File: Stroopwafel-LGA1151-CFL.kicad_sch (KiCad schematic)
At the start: 0 parts

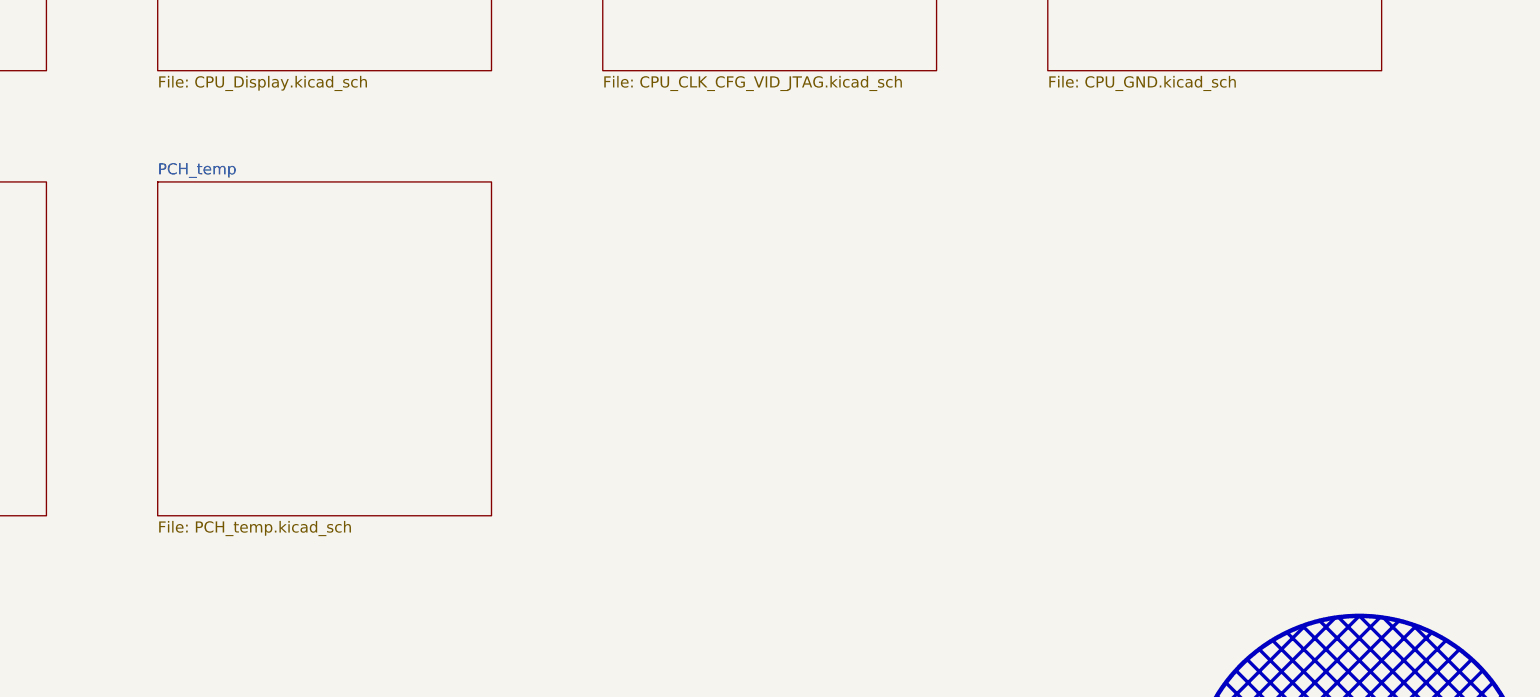
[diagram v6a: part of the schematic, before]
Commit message: Moved PCH symbols to their own pages
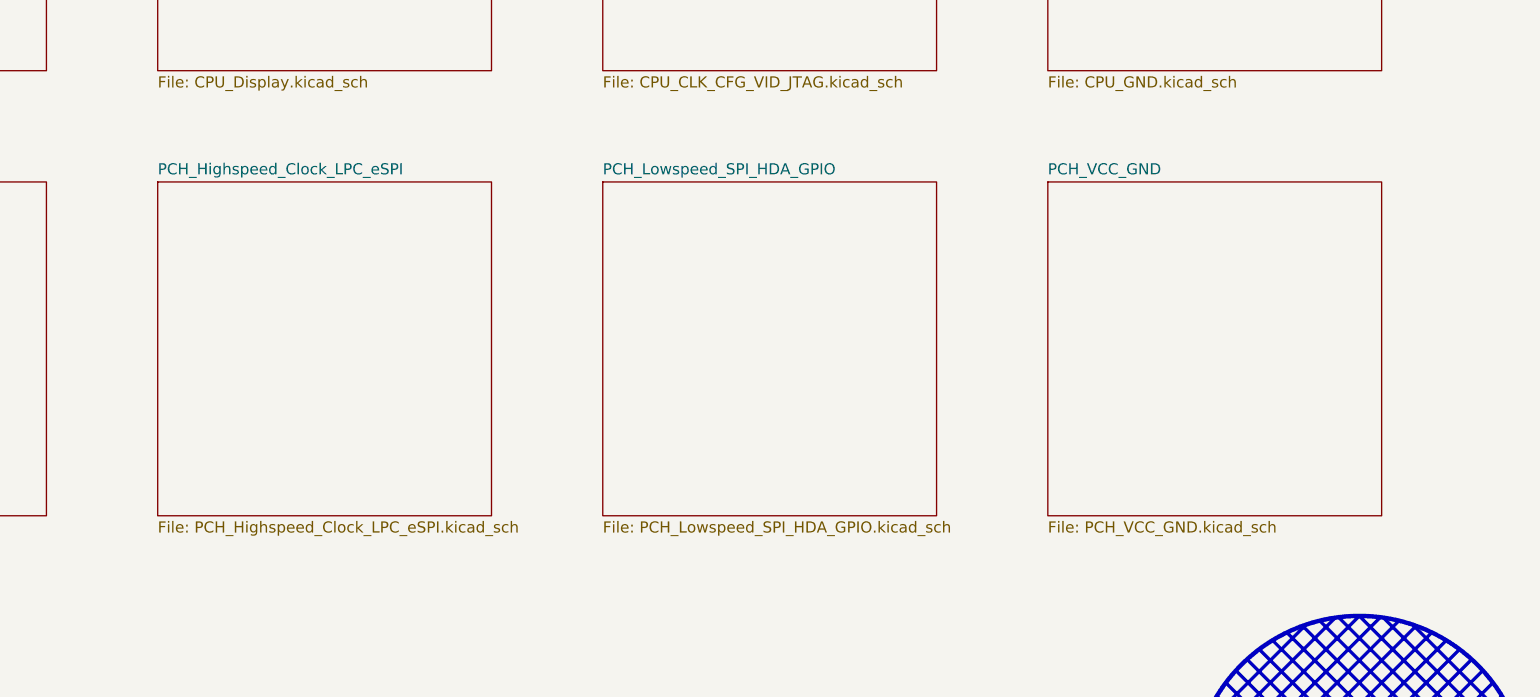
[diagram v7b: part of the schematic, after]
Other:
- removed sheet PCH_temp
- added sheet PCH_Highspeed_Clock_LPC_eSPI (PCH_Highspeed_Clock_LPC_eSPI.kicad_sch)
- added sheet PCH_Lowspeed_SPI_HDA_GPIO (PCH_Lowspeed_SPI_HDA_GPIO.kicad_sch)
- added sheet PCH_VCC_GND (PCH_VCC_GND.kicad_sch)
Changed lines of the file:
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@@
+	)
+	(sheet
+		(at 228.6 76.2)
+		(size 38.1 38.1)
+		(exclude_from_sim no)
+		(in_bom yes)
+		(on_board yes)
+		(dnp no)
+		(fields_autoplaced yes)
+		(stroke
+			(width 0.1524)
+			(type solid)
+		)
+		(fill
+			(color 0 0 0 0.0000)
+		)
+		(property "Sheetname" "PCH_VCC_GND"
+			(at 228.6 75.4884 0)
+			(effects
+				(font
+					(size 1.27 1.27)
+				)
+				(justify left bottom)
+			)
+		)
+		(property "Sheetfile" "PCH_VCC_GND.kicad_sch"
+			(at 228.6 114.8846 0)
+			(effects
+				(font
+					(size 1.27 1.27)
+				)
+				(justify left top)
+			)
+		)
+		(instances
+			(project "Stroopwafel-LGA1151-CFL"
+				(path "/4bc771b8-eb19-46d0-8798-27231a7c6e83"
+					(page "11")
+				)
+			)
+		)
 	)
 	(sheet
@@
 	)
 	(sheet
+		(at 127 76.2)
+		(size 38.1 38.1)
+		(exclude_from_sim no)
+		(in_bom yes)
+		(on_board yes)
+		(dnp no)
+		(fields_autoplaced yes)
+		(stroke
+			(width 0.1524)
+			(type solid)
+		)
+		(fill
+			(color 0 0 0 0.0000)
+		)
+		(property "Sheetname" "PCH_Highspeed_Clock_LPC_eSPI"
+			(at 127 75.4884 0)
+			(effects
+				(font
+					(size 1.27 1.27)
+				)
+				(justify left bottom)
+			)
+		)
+		(property "Sheetfile" "PCH_Highspeed_Clock_LPC_eSPI.kicad_sch"
+			(at 127 114.8846 0)
+			(effects
+				(font
+					(size 1.27 1.27)
+				)
+				(justify left top)
+			)
+		)
+		(instances
+			(project "Stroopwafel-LGA1151-CFL"
+				(path "/4bc771b8-eb19-46d0-8798-27231a7c6e83"
+					(page "9")
+				)
+			)
+		)
+	)
+	(sheet
 		(at 228.6 25.4)
 		(size 38.1 38.1)
@@
 	)
 	(sheet
-		(at 127 76.2)
-		(size 38.1 38.1)
-		(exclude_from_sim no)
-		(in_bom yes)
-		(on_board yes)
-		(dnp no)
-		(fields_autoplaced yes)
-		(stroke
-			(width 0.1524)
-			(type solid)
-		)
-		(fill
-			(color 0 0 0 0.0000)
-		)
-		(property "Sheetname" "PCH_temp"
-			(at 127 75.4884 0)
-			(effects
-				(font
-					(size 1.27 1.27)
-				)
-				(justify left bottom)
-			)
-		)
-		(property "Sheetfile" "PCH_temp.kicad_sch"
-			(at 127 114.8846 0)
-			(effects
-				(font
-					(size 1.27 1.27)
-				)
-				(justify left top)
-			)
-		)
-		(instances
-			(project "Stroopwafel-LGA1151-CFL"
-				(path "/4bc771b8-eb19-46d0-8798-27231a7c6e83"
-					(page "9")
-				)
-			)
+		(at 177.8 76.2)
+		(size 38.1 38.1)
+		(exclude_from_sim no)
+		(in_bom yes)
+		(on_board yes)
+		(dnp no)
+		(fields_autoplaced yes)
+		(stroke
+			(width 0.1524)
+			(type solid)
+		)
+		(fill
+			(color 0 0 0 0.0000)
+		)
+		(property "Sheetname" "PCH_Lowspeed_SPI_HDA_GPIO"
+			(at 177.8 75.4884 0)
+			(effects
+				(font
+					(size 1.27 1.27)
+				)
+				(justify left bottom)
+			)
+		)
+		(property "Sheetfile" "PCH_Lowspeed_SPI_HDA_GPIO.kicad_sch"
+			(at 177.8 114.8846 0)
+			(effects
+				(font
+					(size 1.27 1.27)
+				)
+				(justify left top)
+			)
+		)
+		(instances
+			(project "Stroopwafel-LGA1151-CFL"
+				(path "/4bc771b8-eb19-46d0-8798-27231a7c6e83"
+					(page "10")
+				)
+			)

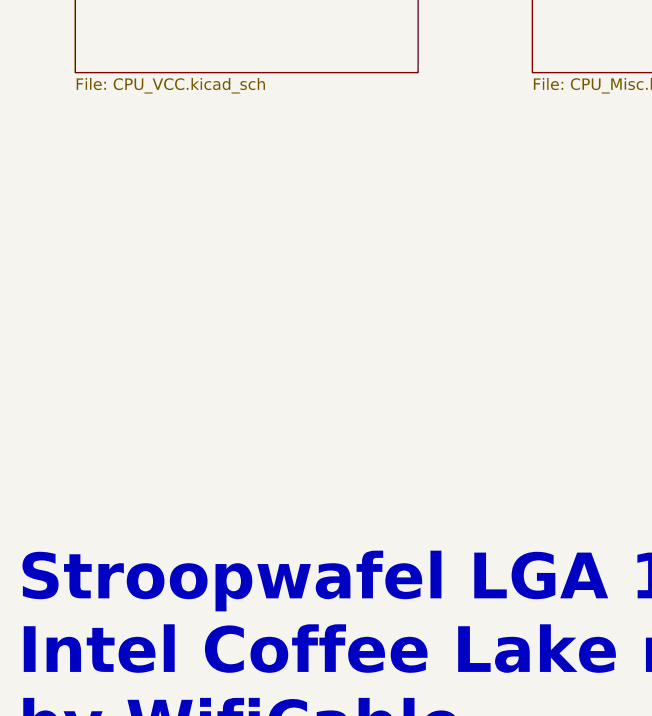
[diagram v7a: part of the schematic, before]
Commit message: Added sodimm memory slots and mostly hooked them up on the schematic
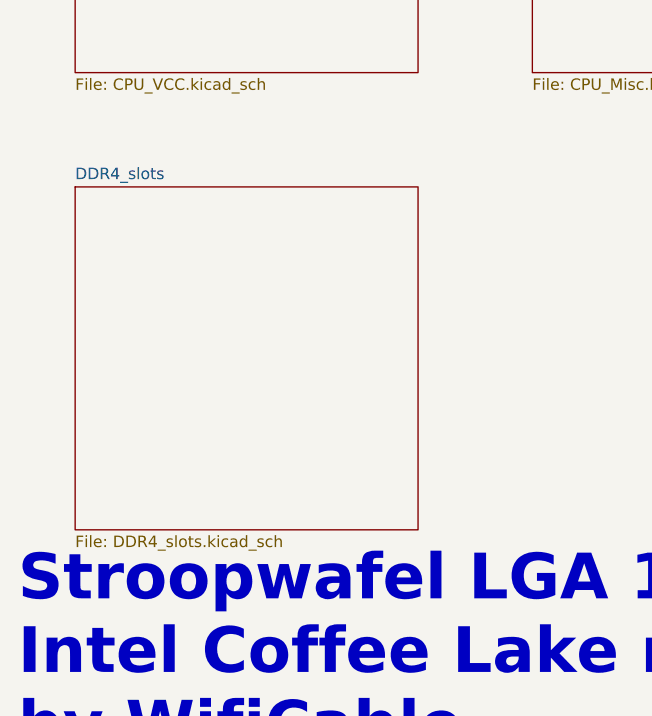
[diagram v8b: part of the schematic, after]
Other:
- added sheet DDR4_slots (DDR4_slots.kicad_sch)
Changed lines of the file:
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@@
+	)
+	(sheet
+		(at 25.4 127)
+		(size 38.1 38.1)
+		(exclude_from_sim no)
+		(in_bom yes)
+		(on_board yes)
+		(dnp no)
+		(fields_autoplaced yes)
+		(stroke
+			(width 0.1524)
+			(type solid)
+		)
+		(fill
+			(color 0 0 0 0.0000)
+		)
+		(property "Sheetname" "DDR4_slots"
+			(at 25.4 126.2884 0)
+			(effects
+				(font
+					(size 1.27 1.27)
+				)
+				(justify left bottom)
+			)
+		)
+		(property "Sheetfile" "DDR4_slots.kicad_sch"
+			(at 25.4 165.6846 0)
+			(effects
+				(font
+					(size 1.27 1.27)
+				)
+				(justify left top)
+			)
+		)
+		(instances
+			(project "Stroopwafel-LGA1151-CFL"
+				(path "/4bc771b8-eb19-46d0-8798-27231a7c6e83"
+					(page "12")
+				)
+			)
+		)
 	)
 	(sheet
